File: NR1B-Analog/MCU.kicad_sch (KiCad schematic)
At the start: 12 parts, among them J3 Conn_01x03_Male, SW1 1-1571636-0, U5 Pico

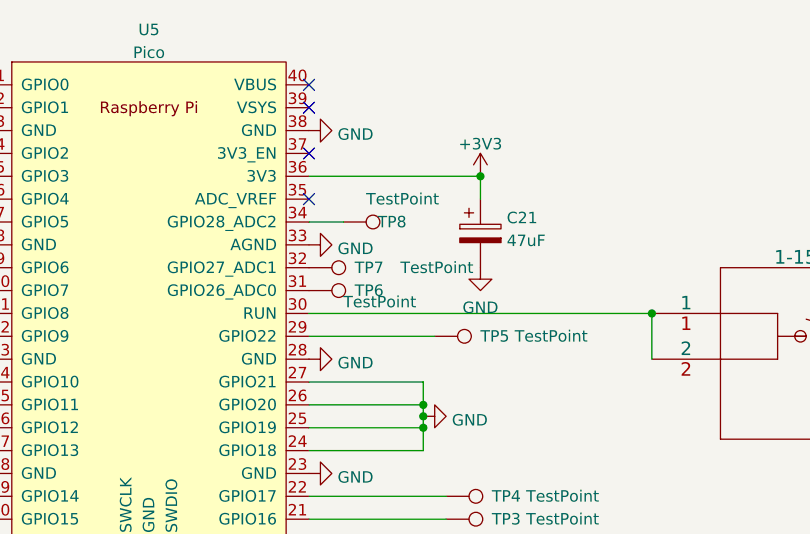
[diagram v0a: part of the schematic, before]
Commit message: Added ADC for voltage reading
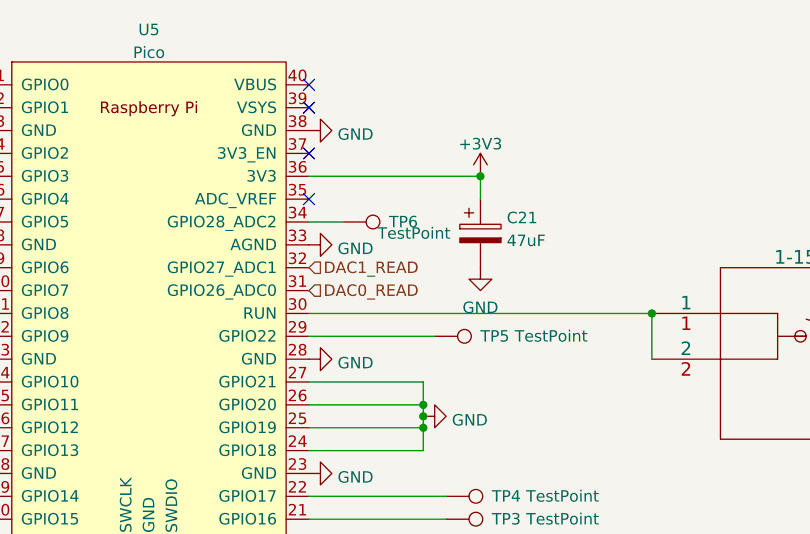
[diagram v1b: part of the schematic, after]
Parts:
- removed TP7, TP8: TestPoint, TestPoint:TestPoint_Bridge_Pitch2.0mm_Drill0.7mm, symbol Connector:TestPoint
- SW1: footprint SW5_1571636_TEC -> 1-1571636-0:1-1571636-0
- U5: footprint RPi_Pico:RPi_Pico_SMD_TH -> MCU_RaspberryPi_and_Boards:RPi_Pico_SMD_TH
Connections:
- net DAC1_READ: now reaches U5.32 (GPIO27_ADC1)
- net at U5.34 (GPIO28_ADC2): now also TP6.1
- net DAC0_READ: now reaches U5.31 (GPIO26_ADC0)
- net DAC0_READ: no longer TP6.1
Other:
- moved on the sheet: TP6
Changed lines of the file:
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@@
     (effects (font (size 1.27 1.27)) (justify right))
+  )
+  (hierarchical_label "DAC0_READ" (shape input) (at 143.51 86.36 0)
+    (effects (font (size 1.27 1.27)) (justify left))
   )
   (hierarchical_label "MOSI_SYS" (shape input) (at 107.95 76.2 180)
@@
   (hierarchical_label "LDAC" (shape input) (at 107.95 104.14 180)
     (effects (font (size 1.27 1.27)) (justify right))
+  )
+  (hierarchical_label "DAC1_READ" (shape input) (at 143.51 83.82 0)
+    (effects (font (size 1.27 1.27)) (justify left))
   )
   (symbol (lib_id "Connector:TestPoint") (at 158.75 109.22 270) (unit 1)
@@
     (pin "1")
   )
-  (symbol (lib_id "Connector:TestPoint") (at 143.51 83.82 270) (unit 1)
-    (in_bom yes) (on_board yes)
-    (property "Reference" "TP7" (id 0) (at 148.59 83.82 90)
-      (effects (font (size 1.27 1.27)) (justify left))
-    )
-    (property "Value" "TestPoint" (id 1) (at 153.67 83.82 90)
-      (effects (font (size 1.27 1.27)) (justify left))
-    )
-    (property "Footprint" "TestPoint:TestPoint_Bridge_Pitch2.0mm_Drill0.7mm" (id 2) (at 143.51 88.9 0)
-      (effects (font (size 1.27 1.27)) hide)
-    )
-    (property "Datasheet" "~" (id 3) (at 143.51 88.9 0)
-      (effects (font (size 1.27 1.27)) hide)
-    )
-    (pin "1")
-  )
-  (symbol (lib_id "Connector:TestPoint") (at 147.32 78.74 270) (unit 1)
-    (in_bom yes) (on_board yes)
-    (property "Reference" "TP8" (id 0) (at 151.13 78.74 90)
-      (effects (font (size 1.27 1.27)) (justify left))
-    )
-    (property "Value" "TestPoint" (id 1) (at 149.86 76.2 90)
-      (effects (font (size 1.27 1.27)) (justify left))
-    )
-    (property "Footprint" "TestPoint:TestPoint_Bridge_Pitch2.0mm_Drill0.7mm" (id 2) (at 147.32 83.82 0)
-      (effects (font (size 1.27 1.27)) hide)
-    )
-    (property "Datasheet" "~" (id 3) (at 147.32 83.82 0)
-      (effects (font (size 1.27 1.27)) hide)
-    )
-    (pin "1")
-  )
   (symbol (lib_id "power:GND") (at 162.56 83.82 0) (unit 1)
     (in_bom yes) (on_board yes) (fields_autoplaced)
@@
     (pin "1")
   )
-  (symbol (lib_id "Connector:TestPoint") (at 143.51 86.36 270) (unit 1)
-    (in_bom yes) (on_board yes)
-    (property "Reference" "TP6" (id 0) (at 148.59 86.36 90)
-      (effects (font (size 1.27 1.27)) (justify left))
-    )
-    (property "Value" "TestPoint" (id 1) (at 147.32 87.63 90)
-      (effects (font (size 1.27 1.27)) (justify left))
-    )
-    (property "Footprint" "TestPoint:TestPoint_Bridge_Pitch2.0mm_Drill0.7mm" (id 2) (at 143.51 91.44 0)
-      (effects (font (size 1.27 1.27)) hide)
-    )
-    (property "Datasheet" "~" (id 3) (at 143.51 91.44 0)
+  (symbol (lib_id "Connector:TestPoint") (at 147.32 78.74 270) (unit 1)
+    (in_bom yes) (on_board yes)
+    (property "Reference" "TP6" (id 0) (at 152.4 78.74 90)
+      (effects (font (size 1.27 1.27)) (justify left))
+    )
+    (property "Value" "TestPoint" (id 1) (at 151.13 80.01 90)
+      (effects (font (size 1.27 1.27)) (justify left))
+    )
+    (property "Footprint" "TestPoint:TestPoint_Bridge_Pitch2.0mm_Drill0.7mm" (id 2) (at 147.32 83.82 0)
+      (effects (font (size 1.27 1.27)) hide)
+    )
+    (property "Datasheet" "~" (id 3) (at 147.32 83.82 0)
       (effects (font (size 1.27 1.27)) hide)
     )
@@
       (effects (font (size 1.524 1.524)))
     )
-    (property "Footprint" "SW5_1571636_TEC" (id 2) (at 201.93 82.804 0)
+    (property "Footprint" "1-1571636-0:1-1571636-0" (id 2) (at 201.93 82.804 0)
       (effects (font (size 1.524 1.524)) hide)
     )
@@
     (property "Reference" "U5" (id 0) (at 125.73 57.3872 0))
     (property "Value" "Pico" (id 1) (at 125.73 59.9241 0))
-    (property "Footprint" "RPi_Pico:RPi_Pico_SMD_TH" (id 2) (at 125.73 87.63 90)
-      (effects (font (size 1.27 1.27)) hide)
-    )
+    (property "Footprint" "MCU_RaspberryPi_and_Boards:RPi_Pico_SMD_TH" (id 2) (at 125.73 87.63 90)
+      (effects (font (size 1.27 1.27)) hide)
+    )

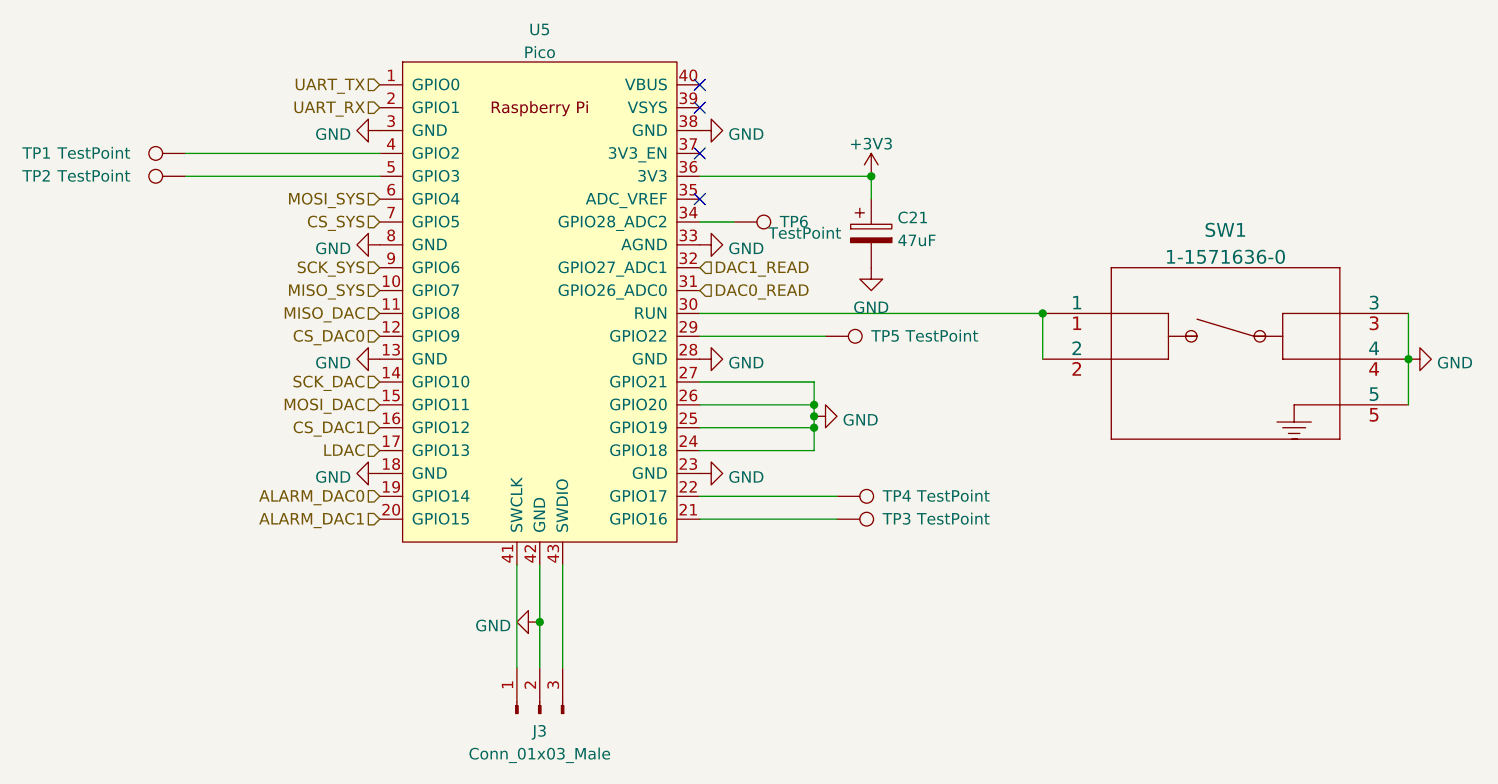
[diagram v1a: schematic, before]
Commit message: Fixed symbol libs, see notes from July 25 on PCB and schema
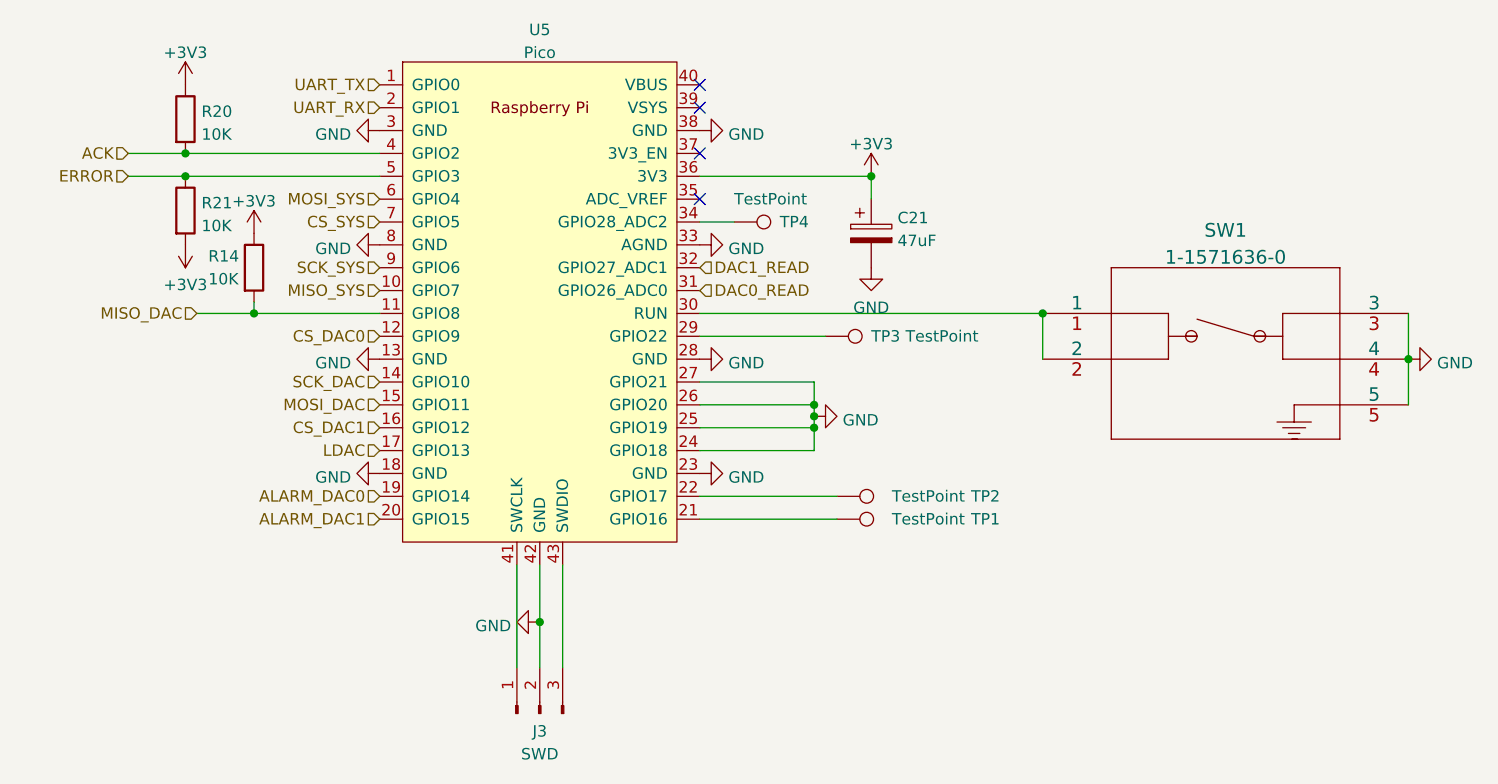
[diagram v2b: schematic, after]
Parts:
- removed TP5, TP6: TestPoint, TestPoint:TestPoint_Bridge_Pitch2.0mm_Drill0.7mm, symbol Connector:TestPoint
- added R14, R20, R21: 10K, Resistor_SMD:R_0603_1608Metric, symbol Device:R
- J3: value Conn_01x03_Male -> SWD
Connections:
- net +3V3: now also R14.1, R20.1, R21.2
- net MISO_DAC: now also R14.2
- net at TP4.1: now also U5.34 (GPIO28_ADC2); no longer U5.22 (GPIO17)
- net at TP2.1: now also U5.22 (GPIO17); no longer U5.5 (GPIO3)
- net at TP3.1: now also U5.29 (GPIO22); no longer U5.21 (GPIO16)
- net at TP1.1: now also U5.21 (GPIO16); no longer U5.4 (GPIO2)
- new net ACK: R20.2, U5.4 (GPIO2)
- new net ERROR: R21.1, U5.5 (GPIO3)
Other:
- moved on the sheet: TP1, TP2, TP3, TP4

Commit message: Labeled sheets, adjusted pot location
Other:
- company: (none) -> University of Dallas
- title: (none) -> NR1B-Analog
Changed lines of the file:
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@@
 (kicad_sch (version 20211123) (generator eeschema)
   (paper "A4")
+  (title_block
+    (title "NR1B-Analog")
+    (date "2022-07-26")
+    (rev "v1.0")
+    (company "University of Dallas")
+    (comment 1 "Isaac Kelly")
+  )
   (junction (at 156.21 101.6) (diameter 0) (color 0 0 0 0)
   )

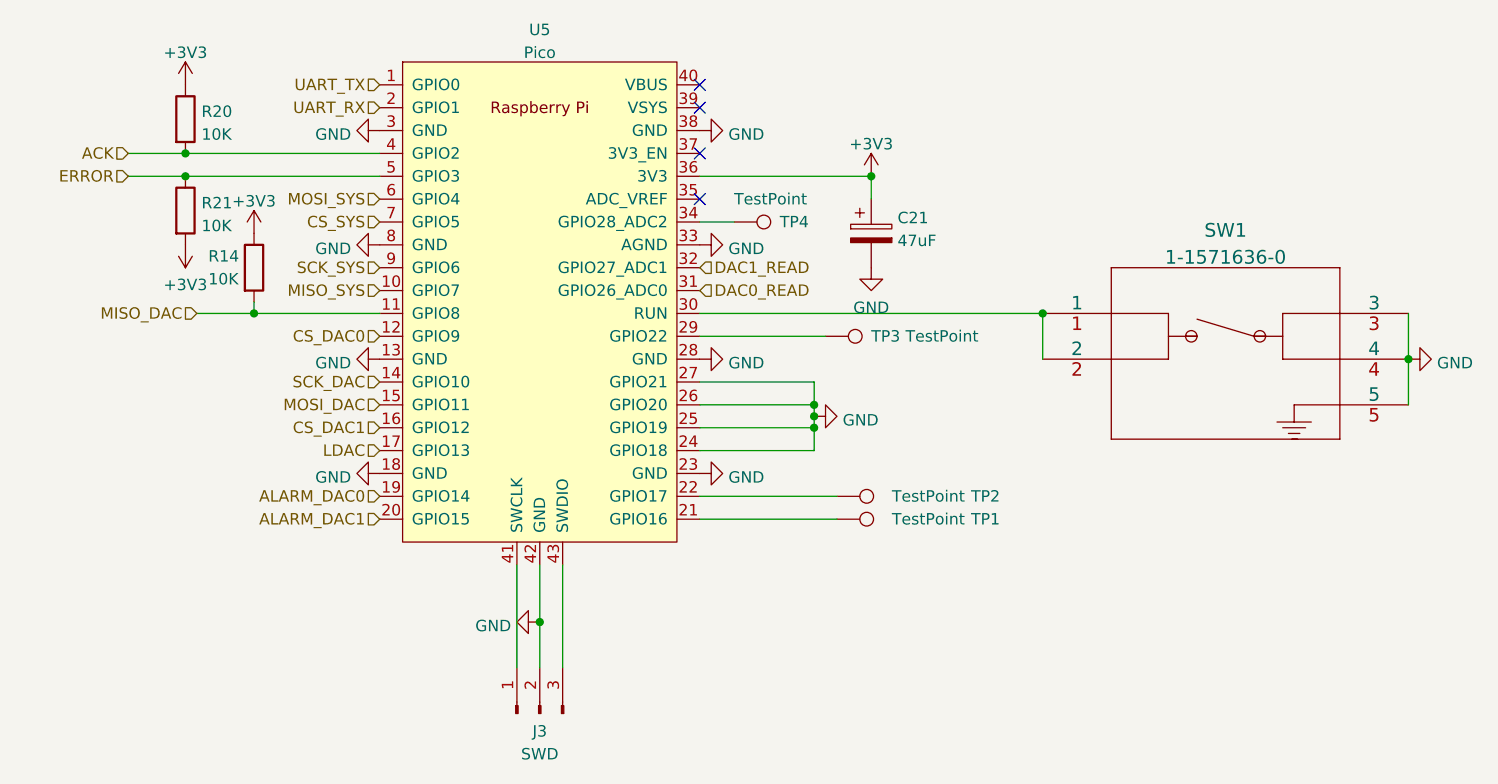
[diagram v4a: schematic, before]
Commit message: Changed footprints, re-routed
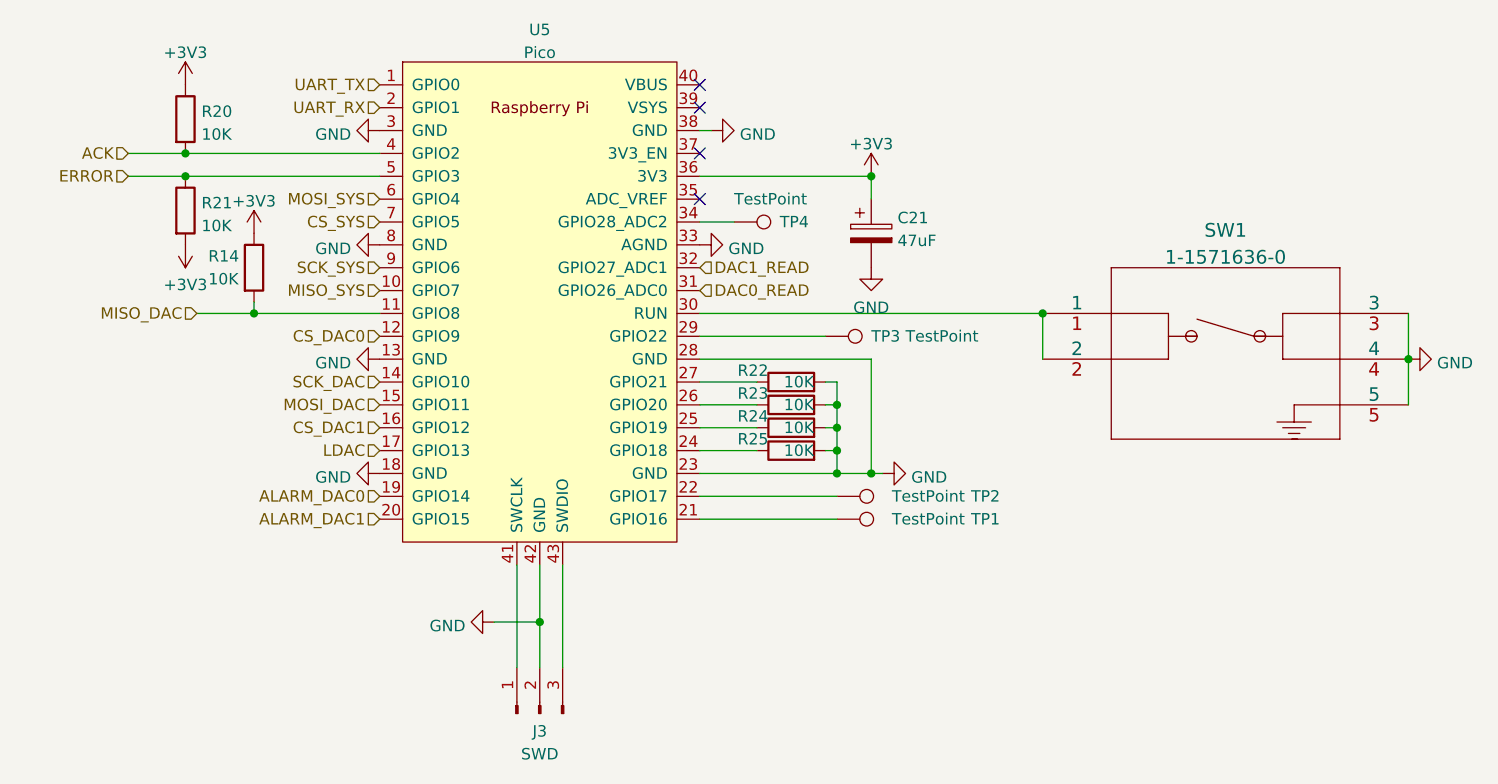
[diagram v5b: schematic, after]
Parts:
- added R22, R23, R24, R25: 10K, Resistor_SMD:R_0603_1608Metric, symbol Device:R
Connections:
- net GND: now also R22.2, R23.2, R24.2, R25.2; no longer U5.24 (GPIO18), U5.25 (GPIO19), U5.26 (GPIO20), U5.27 (GPIO21)
- new net: R23.1, U5.26 (GPIO20)
- new net: R24.1, U5.25 (GPIO19)
- new net: R22.1, U5.27 (GPIO21)
- new net: R25.1, U5.24 (GPIO18)
